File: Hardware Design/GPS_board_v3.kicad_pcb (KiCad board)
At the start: 2 copper layers, 50 x 77.5 mm, 19 parts, among them IC2 SN65HVD231QDR, U1 STM32F042F4Px, U5 MAX-M8W

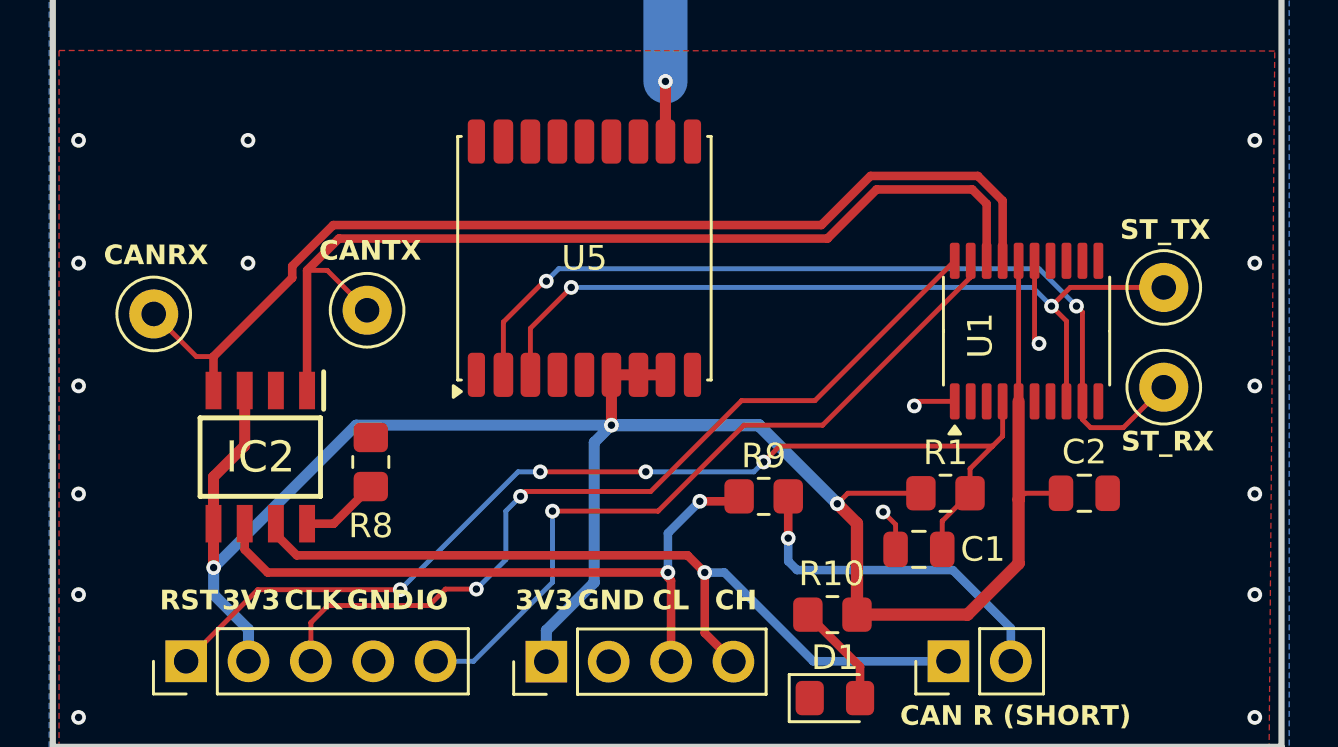
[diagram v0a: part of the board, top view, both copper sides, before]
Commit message: Added testing headers.
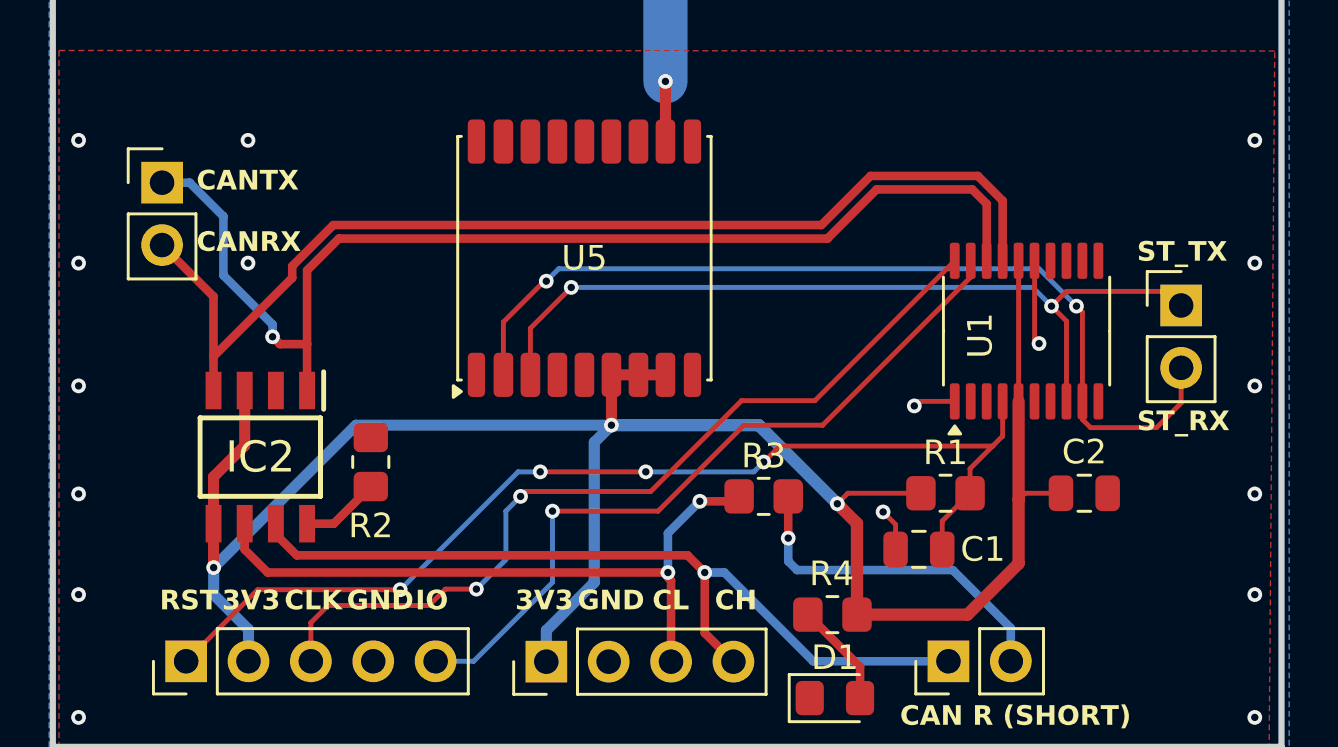
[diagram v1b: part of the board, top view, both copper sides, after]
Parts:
- removed REF** (x4): TestPoint_Loop_D2.50mm_Drill1.0mm_LowProfile, TestPoint:TestPoint_Loop_D2.50mm_Drill1.0mm_LowProfile
- added J1: STM-UART, Connector_PinHeader_2.54mm:PinHeader_1x02_P2.54mm_Vertical, F.Cu at (168.6, 111.2)
- added J5: STM-UART, Connector_PinHeader_2.54mm:PinHeader_1x02_P2.54mm_Vertical, F.Cu at (127.1, 106.2)
- renumbered R8 to R2, R9 to R3, R10 to R4
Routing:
- net CAN_TX: track 39.6 -> 46.8 mm, vias 0 -> 1
- net CAN_RX: track 42.9 -> 45.1 mm
- net STM_UART_RX: track 35.9 -> 37.7 mm
- net STM_UART_TX: track 33.1 -> 34.0 mm
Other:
- board text added: "Designed By: Paul Scalise University of Nebraska-Lincoln"
- board text removed: "Designed By: Paul Scalise"
